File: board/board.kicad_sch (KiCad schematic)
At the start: 3 parts, among them J1 002_SPI, J2 007_ADC

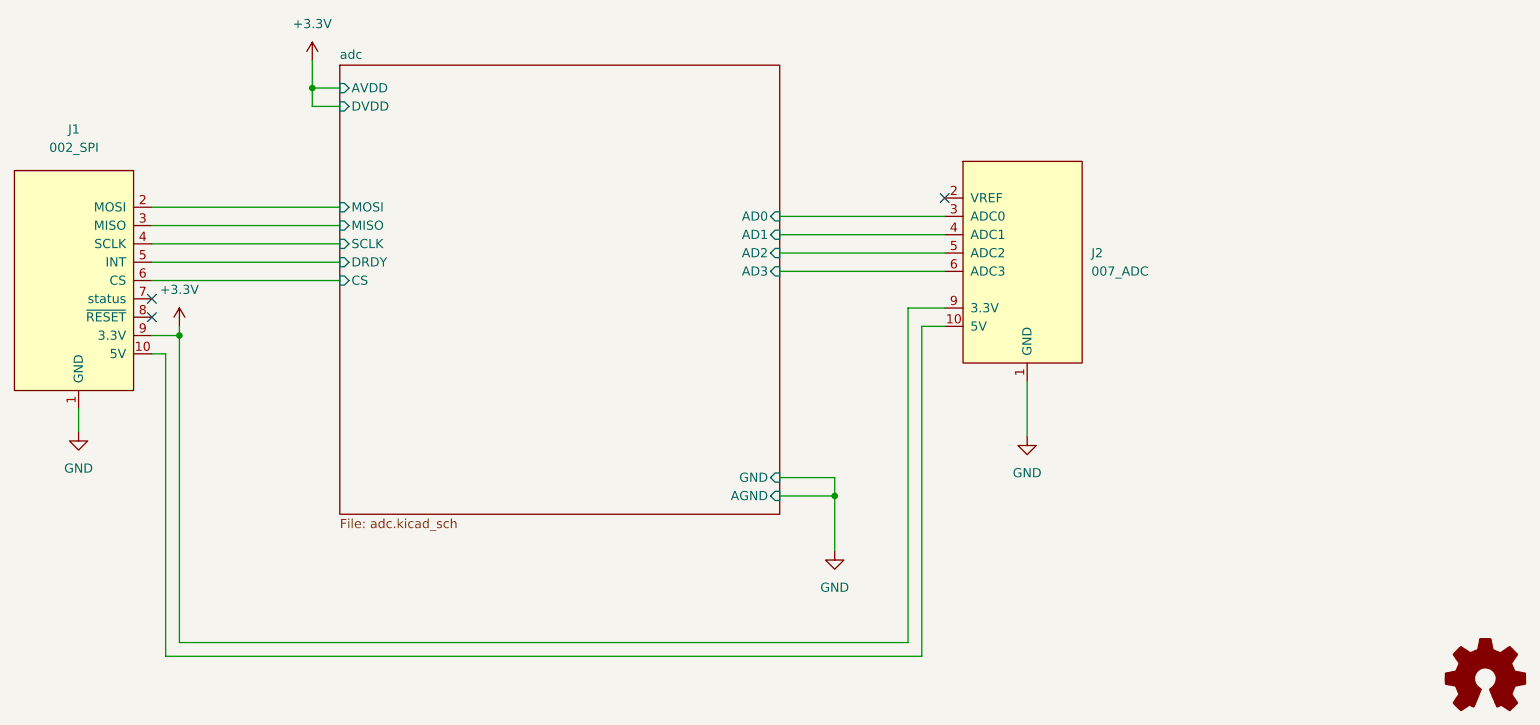
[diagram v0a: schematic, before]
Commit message: added jlc production files and some cosmetic changes
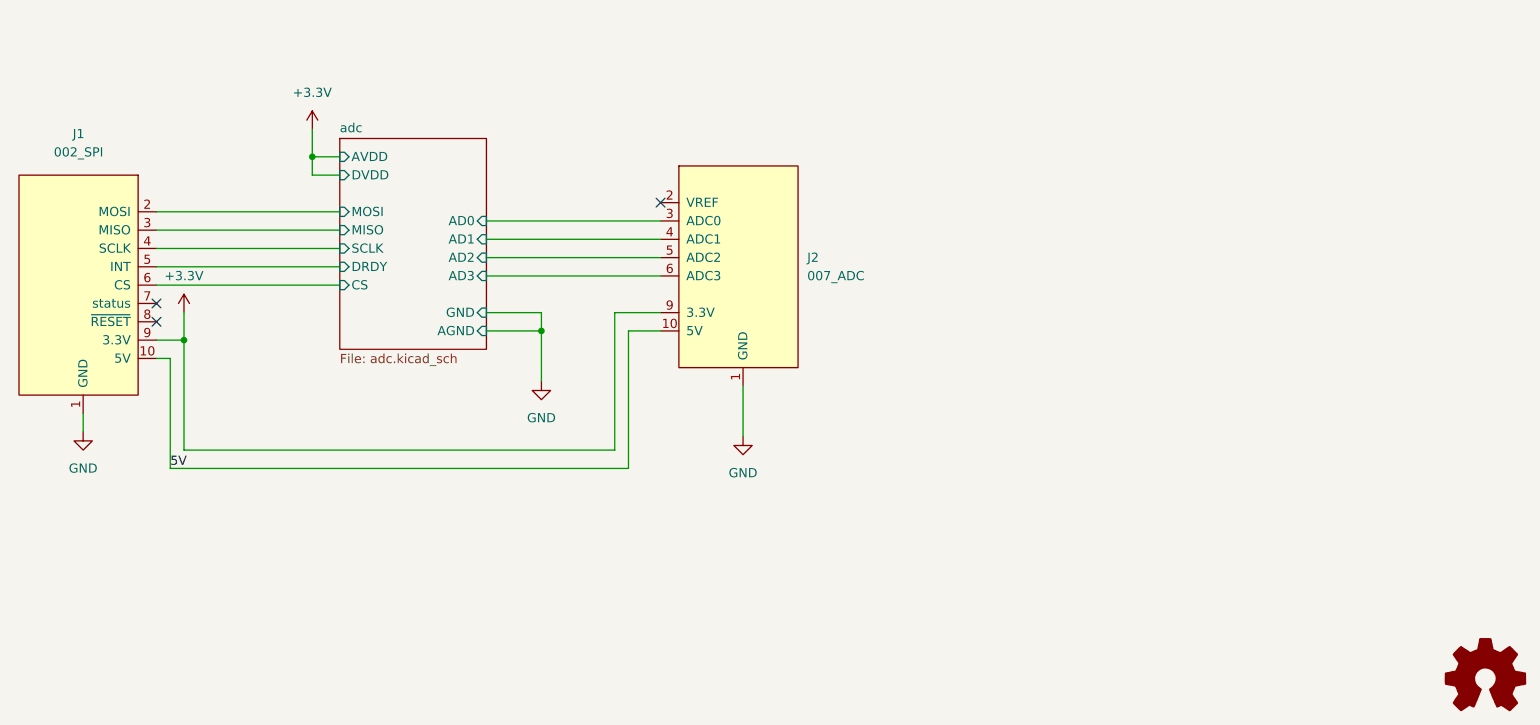
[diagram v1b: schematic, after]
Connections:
- net 5V: now reaches J1.10 (5V), J2.10 (5V)
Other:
- moved on the sheet: J1, J2
